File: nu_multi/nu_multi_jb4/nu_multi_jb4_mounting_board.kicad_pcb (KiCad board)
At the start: 2 copper layers, 78.5 x 18 mm, 6 parts, among them J13 CONN_01X14, U1 nu_capsule, U2 nu_capsule, U3 nu_capsule, U4 nu_capsule

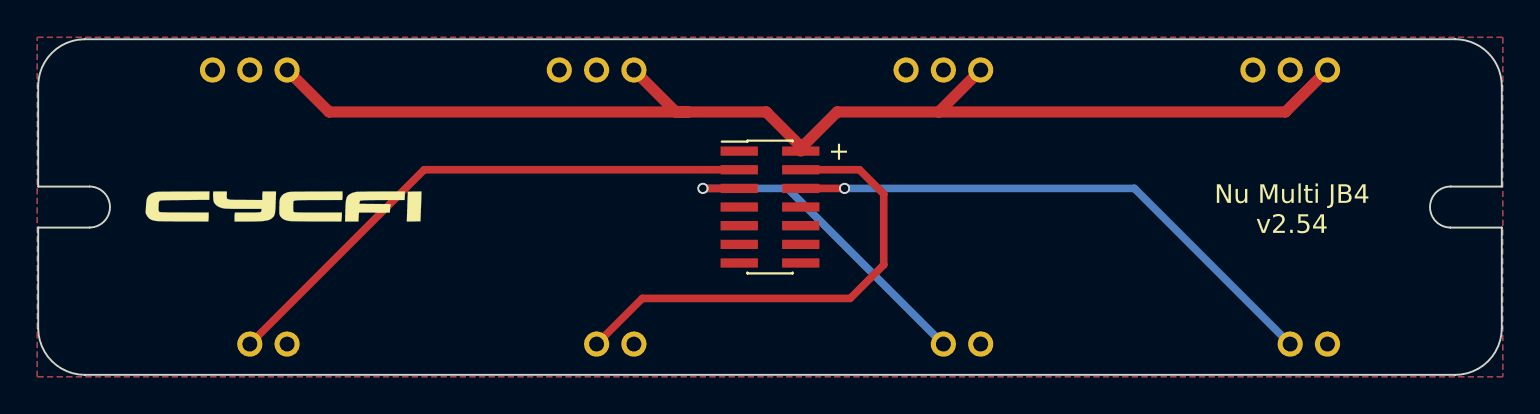
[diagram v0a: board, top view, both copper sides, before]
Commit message: Updated PCB mounting board and drawing guide
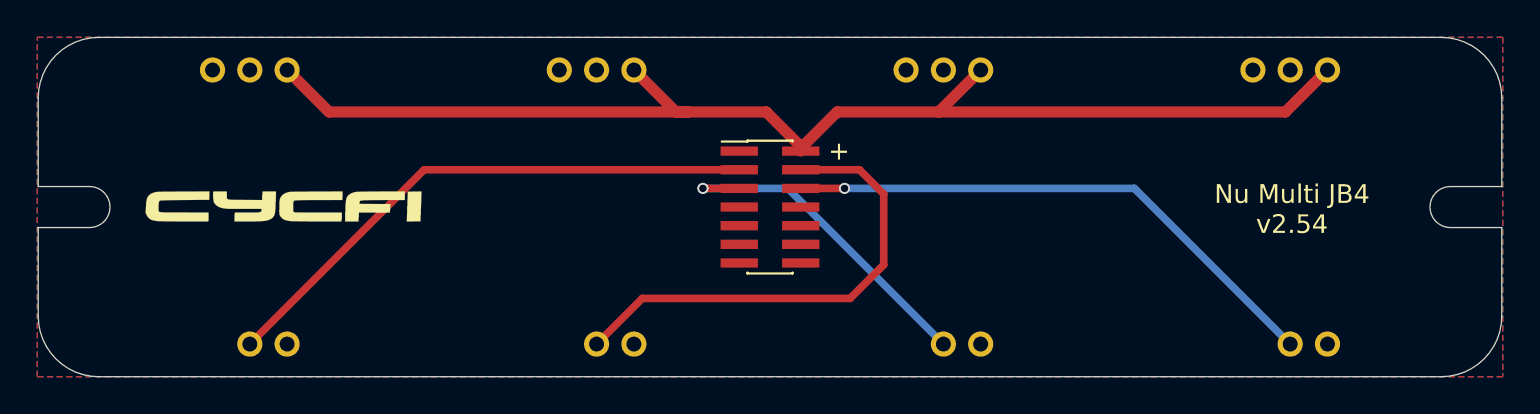
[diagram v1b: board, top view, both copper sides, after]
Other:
- board size 78.5 x 18 mm -> 78.5 x 18.2 mm
